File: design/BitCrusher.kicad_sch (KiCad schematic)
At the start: 0 parts

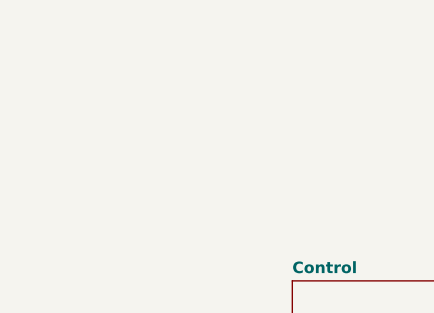
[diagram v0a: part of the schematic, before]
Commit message: Working on GaNFET driver circuit for HV switching
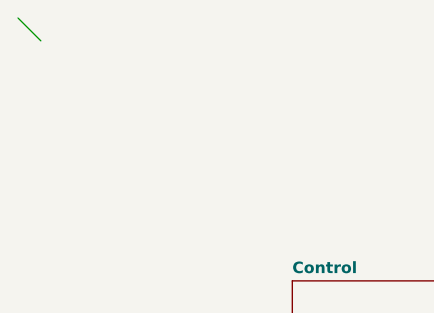
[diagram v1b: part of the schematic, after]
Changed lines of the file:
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@@
 		(comment 2 "Author: George Crane")
+	)
+	(bus_entry
+		(at 0 0)
+		(size 2.54 2.54)
+		(stroke
+			(width 0)
+			(type default)
+		)
 	)
 	(sheet

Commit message: Working on high voltage switching
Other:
- company: UNH Resilient Architecture Lab -> University of New Hampshire, Resilient Architecture Lab
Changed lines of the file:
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@@
 		(title "BitCrusher: Affordable, Open Source EMFI Platform")
 		(rev "0.1")
-		(company "UNH Resilient Architecture Lab")
+		(company "University of New Hampshire, Resilient Architecture Lab")
 		(comment 1 "Advisor: Dean Sullivan")
 		(comment 2 "Author: George Crane")
@@
 			(project "BitCrusher"
 				(path "/e1be550d-9ce6-42b1-a89a-c00b9d7586dd"
-					(page "6")
+					(page "5")
 				)
 			)

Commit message: Almost done with layout
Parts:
- added H1, H2, H3, H4: MountingHole, MountingHole:MountingHole_3.2mm_M3, symbol Mechanical:MountingHole

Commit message: _
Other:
- sheet Control renamed Control & Interface
- sheet Primary Power renamed Primary Power Distribution
- moved on the sheet: H1, H2, H3, H4
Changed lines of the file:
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@@
 	(symbol
 		(lib_id "Mechanical:MountingHole")
-		(at 31.75 132.08 0)
+		(at 31.75 170.18 0)
 		(unit 1)
 		(exclude_from_sim no)
@@
 		(fields_autoplaced yes)
 		(property "Reference" "H2"
-			(at 34.29 130.8099 0)
+			(at 34.29 168.9099 0)
 			(effects
 				(font
@@
 		)
 		(property "Value" "MountingHole"
-			(at 34.29 133.3499 0)
+			(at 34.29 171.4499 0)
 			(effects
 				(font
@@
 		)
 		(property "Footprint" "MountingHole:MountingHole_3.2mm_M3"
-			(at 31.75 132.08 0)
+			(at 31.75 170.18 0)
 			(effects
 				(font
@@
 		)
 		(property "Datasheet" "~"
-			(at 31.75 132.08 0)
+			(at 31.75 170.18 0)
 			(effects
 				(font
@@
 		)
 		(property "Description" "Mounting Hole without connection"
-			(at 31.75 132.08 0)
+			(at 31.75 170.18 0)
+			(effects
+				(font
+					(size 1.27 1.27)
+				)
+				(hide yes)
+			)
+		)
+		(property "KLC_S4.2_3V3OUT" ""
+			(at 31.75 170.18 0)
+			(effects
+				(font
+					(size 1.27 1.27)
+				)
+				(hide yes)
+			)
+		)
+		(property "KLC_S4.2_VCC" ""
+			(at 31.75 170.18 0)
 			(effects
 				(font
@@
 	(symbol
 		(lib_id "Mechanical:MountingHole")
-		(at 31.75 127 0)
+		(at 31.75 165.1 0)
 		(unit 1)
 		(exclude_from_sim no)
@@
 		(fields_autoplaced yes)
 		(property "Reference" "H1"
-			(at 34.29 125.7299 0)
+			(at 34.29 163.8299 0)
 			(effects
 				(font
@@
 		)
 		(property "Value" "MountingHole"
-			(at 34.29 128.2699 0)
+			(at 34.29 166.3699 0)
 			(effects
 				(font
@@
 		)
 		(property "Footprint" "MountingHole:MountingHole_3.2mm_M3"
-			(at 31.75 127 0)
+			(at 31.75 165.1 0)
 			(effects
 				(font
@@
 		)
 		(property "Datasheet" "~"
-			(at 31.75 127 0)
+			(at 31.75 165.1 0)
 			(effects
 				(font
@@
 		)
 		(property "Description" "Mounting Hole without connection"
-			(at 31.75 127 0)
+			(at 31.75 165.1 0)
+			(effects
+				(font
+					(size 1.27 1.27)
+				)
+				(hide yes)
+			)
+		)
+		(property "KLC_S4.2_3V3OUT" ""
+			(at 31.75 165.1 0)
+			(effects
+				(font
+					(size 1.27 1.27)
+				)
+				(hide yes)
+			)
+		)
+		(property "KLC_S4.2_VCC" ""
+			(at 31.75 165.1 0)
 			(effects
 				(font
@@
 	(symbol
 		(lib_id "Mechanical:MountingHole")
-		(at 31.75 142.24 0)
+		(at 31.75 180.34 0)
 		(unit 1)
 		(exclude_from_sim no)
@@
 		(fields_autoplaced yes)
 		(property "Reference" "H4"
-			(at 34.29 140.9699 0)
+			(at 34.29 179.0699 0)
 			(effects
 				(font
@@
 		)
 		(property "Value" "MountingHole"
-			(at 34.29 143.5099 0)
+			(at 34.29 181.6099 0)
 			(effects
 				(font
@@
 		)
 		(property "Footprint" "MountingHole:MountingHole_3.2mm_M3"
-			(at 31.75 142.24 0)
+			(at 31.75 180.34 0)
 			(effects
 				(font
@@
 		)
 		(property "Datasheet" "~"
-			(at 31.75 142.24 0)
+			(at 31.75 180.34 0)
 			(effects
 				(font
@@
 		)
 		(property "Description" "Mounting Hole without connection"
-			(at 31.75 142.24 0)
+			(at 31.75 180.34 0)
+			(effects
+				(font
+					(size 1.27 1.27)
+				)
+				(hide yes)
+			)
+		)
+		(property "KLC_S4.2_3V3OUT" ""
+			(at 31.75 180.34 0)
+			(effects
+				(font
+					(size 1.27 1.27)
+				)
+				(hide yes)
+			)
+		)
+		(property "KLC_S4.2_VCC" ""
+			(at 31.75 180.34 0)
 			(effects
 				(font
@@
 	(symbol
 		(lib_id "Mechanical:MountingHole")
-		(at 31.75 137.16 0)
+		(at 31.75 175.26 0)
 		(unit 1)
 		(exclude_from_sim no)
@@
 		(fields_autoplaced yes)
 		(property "Reference" "H3"
-			(at 34.29 135.8899 0)
+			(at 34.29 173.9899 0)
 			(effects
 				(font
@@
 		)
 		(property "Value" "MountingHole"
-			(at 34.29 138.4299 0)
+			(at 34.29 176.5299 0)
 			(effects
 				(font
@@
 		)
 		(property "Footprint" "MountingHole:MountingHole_3.2mm_M3"
-			(at 31.75 137.16 0)
+			(at 31.75 175.26 0)
 			(effects
 				(font
@@
 		)
 		(property "Datasheet" "~"
-			(at 31.75 137.16 0)
+			(at 31.75 175.26 0)
 			(effects
 				(font
@@
 		)
 		(property "Description" "Mounting Hole without connection"
-			(at 31.75 137.16 0)
+			(at 31.75 175.26 0)
+			(effects
+				(font
+					(size 1.27 1.27)
+				)
+				(hide yes)
+			)
+		)
+		(property "KLC_S4.2_3V3OUT" ""
+			(at 31.75 175.26 0)
+			(effects
+				(font
+					(size 1.27 1.27)
+				)
+				(hide yes)
+			)
+		)
+		(property "KLC_S4.2_VCC" ""
+			(at 31.75 175.26 0)
 			(effects
 				(font
@@
 	)
 	(sheet
-		(at 30.48 68.58)
-		(size 34.29 27.94)
+		(at 100.965 29.21)
+		(size 34.29 53.34)
 		(exclude_from_sim no)
 		(in_bom yes)
 		(on_board yes)
 		(dnp no)
-		(fields_autoplaced yes)
 		(stroke
 			(width 0.1524)
@@
 		)
 		(property "Sheetname" "High Voltage Generation"
-			(at 30.48 67.8684 0)
+			(at 101.092 28.321 0)
 			(effects
 				(font
@@
 		)
 		(property "Sheetfile" "hv-gen.kicad_sch"
-			(at 30.48 97.1046 0)
+			(at 101.092 82.804 0)
 			(effects
 				(font
@@
 	(sheet
 		(at 30.48 29.21)
-		(size 34.29 30.48)
+		(size 58.42 53.34)
 		(exclude_from_sim no)
 		(in_bom yes)
@@
 			(color 0 0 0 0.0000)
 		)
-		(property "Sheetname" "Control"
+		(property "Sheetname" "Control & Interface"
 			(at 30.48 28.4984 0)
 			(effects
@@
 		)
 		(property "Sheetfile" "control.kicad_sch"
-			(at 30.48 60.2746 0)
+			(at 30.48 83.1346 0)
 			(effects
 				(font
@@
 	)
 	(sheet
-		(at 69.85 68.58)
-		(size 33.02 27.94)
+		(at 147.32 29.21)
+		(size 34.29 53.34)
 		(exclude_from_sim no)
 		(in_bom yes)
@@
 		)
 		(property "Sheetname" "High Voltage Switching"
-			(at 69.85 67.8684 0)
+			(at 147.32 28.4984 0)
 			(effects
 				(font
@@
 		)
 		(property "Sheetfile" "hv-switch.kicad_sch"
-			(at 69.85 97.1046 0)
+			(at 147.32 83.1346 0)
 			(effects
 				(font
@@
 	)
 	(sheet
-		(at 69.85 29.21)
-		(size 33.02 30.48)
+		(at 30.48 95.885)
+		(size 58.42 30.48)
 		(exclude_from_sim no)
 		(in_bom yes)
@@
 			(color 0 0 0 0.0000)
 		)
-		(property "Sheetname" "Primary Power"
-			(at 69.85 28.4984 0)
+		(property "Sheetname" "Primary Power Distribution"
+			(at 30.48 95.1734 0)
 			(effects
 				(font
@@
 		)
 		(property "Sheetfile" "power.kicad_sch"
-			(at 69.85 60.2746 0)
-			(effects
-				(font
+			(at 30.48 126.9496 0)
+			(effects
+				(font
